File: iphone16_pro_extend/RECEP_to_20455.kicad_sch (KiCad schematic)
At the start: 7 parts, among them CN1 20455-020E-02

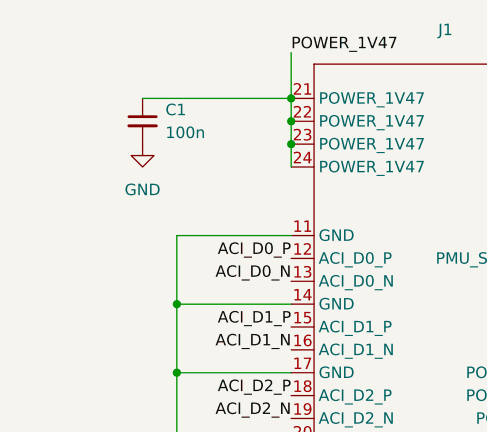
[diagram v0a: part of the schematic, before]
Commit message: Change via diameter to 0.3/0.4mm, reroute
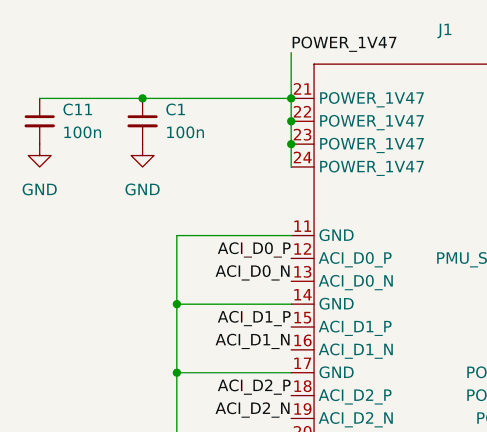
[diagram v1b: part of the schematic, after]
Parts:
- added C11: 100n, Capacitor_SMD:C_0603_1608Metric, symbol Device:C_Small
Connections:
- net GND: now also C11.2
- net POWER_1V47: now also C11.1
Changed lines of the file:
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@@
 	(paper "A4")
+	(junction
+		(at 41.91 45.72)
+		(diameter 0)
+		(color 0 0 0 0)
+	)
 	(junction
 		(at 45.72 83.82)
@@
 		(pts
 			(xy 119.38 53.34) (xy 138.43 53.34)
+		)
+		(stroke
+			(width 0)
+			(type default)
+		)
+	)
+	(wire
+		(pts
+			(xy 30.48 45.72) (xy 41.91 45.72)
 		)
 		(stroke
@@
 	(symbol
 		(lib_id "Device:C_Small")
+		(at 30.48 48.26 0)
+		(unit 1)
+		(body_style 1)
+		(exclude_from_sim no)
+		(in_bom yes)
+		(on_board yes)
+		(in_pos_files yes)
+		(dnp no)
+		(fields_autoplaced yes)
+		(property "Reference" "C11"
+			(at 33.02 46.9962 0)
+			(show_name no)
+			(do_not_autoplace no)
+			(effects
+				(font
+					(size 1.27 1.27)
+				)
+				(justify left)
+			)
+		)
+		(property "Value" "100n"
+			(at 33.02 49.5362 0)
+			(show_name no)
+			(do_not_autoplace no)
+			(effects
+				(font
+					(size 1.27 1.27)
+				)
+				(justify left)
+			)
+		)
+		(property "Footprint" "Capacitor_SMD:C_0603_1608Metric"
+			(at 30.48 48.26 0)
+			(hide yes)
+			(show_name no)
+			(do_not_autoplace no)
+			(effects
+				(font
+					(size 1.27 1.27)
+				)
+			)
+		)
+		(property "Datasheet" ""
+			(at 30.48 48.26 0)
+			(hide yes)
+			(show_name no)
+			(do_not_autoplace no)
+			(effects
+				(font
+					(size 1.27 1.27)
+				)
+			)
+		)
+		(property "Description" "Unpolarized capacitor, small symbol"
+			(at 30.48 48.26 0)
+			(hide yes)
+			(show_name no)
+			(do_not_autoplace no)
+			(effects
+				(font
+					(size 1.27 1.27)
+				)
+			)
+		)
+		(pin "2"
+		)
+		(pin "1"
+		)
+		(instances
+			(project "iphone16_pro_extend"
+				(path "/42fe99c7-182d-4f18-88bd-9b47921653c8/6d5df5d2-7541-4967-a257-6c65f5dcb070"
+					(reference "C11")
+					(unit 1)
+				)
+			)
+		)
+	)
+	(symbol
+		(lib_id "Device:C_Small")
 		(at 41.91 48.26 0)
 		(unit 1)
@@
 					(unit 1)
 				)
+			)
+		)
+	)
+	(symbol
+		(lib_id "power:GND")
+		(at 30.48 50.8 0)
+		(unit 1)
+		(body_style 1)
+		(exclude_from_sim no)
+		(in_bom yes)
+		(on_board yes)
+		(in_pos_files yes)
+		(dnp no)
+		(fields_autoplaced yes)
+		(property "Reference" "#PWR03"
+			(at 30.48 57.15 0)
+			(hide yes)
+			(show_name no)
+			(do_not_autoplace no)
+			(effects
+				(font
+					(size 1.27 1.27)
+				)
+			)
+		)
+		(property "Value" "GND"
+			(at 30.48 55.88 0)
+			(show_name no)
+			(do_not_autoplace no)
+			(effects
+				(font
+					(size 1.27 1.27)
+				)
+			)
+		)
+		(property "Footprint" ""
+			(at 30.48 50.8 0)
+			(hide yes)
+			(show_name no)
+			(do_not_autoplace no)
+			(effects
+				(font
+					(size 1.27 1.27)
+				)
+			)
+		)
+		(property "Datasheet" ""
+			(at 30.48 50.8 0)
+			(hide yes)
+			(show_name no)
+			(do_not_autoplace no)
+			(effects
+				(font
+					(size 1.27 1.27)
+				)
+			)
+		)
+		(property "Description" "Power symbol creates a global label with name \"GND\" , ground"
+			(at 30.48 50.8 0)
+			(hide yes)
+			(show_name no)
+			(do_not_autoplace no)
+			(effects
+				(font
+					(size 1.27 1.27)
+				)
+			)
+		)
+		(pin "1"
+		)
+		(instances
+			(project "iphone16_pro_extend"
+				(path "/42fe99c7-182d-4f18-88bd-9b47921653c8/6d5df5d2-7541-4967-a257-6c65f5dcb070"
+					(reference "#PWR03")
+					(unit 1)
+				)
